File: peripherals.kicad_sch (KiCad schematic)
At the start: 27 parts, among them J7 Conn_01x04, J8 Conn_01x06, J9 Conn_01x06, U11 TB6612FNG, U2 LSM6DSV

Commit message: Use basic parts where possible
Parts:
- C2, C32, C36, C37, C38, C39: footprint Capacitor_SMD:C_0603_1608Metric_Pad1.08x0.95mm_HandSolder -> Capacitor_SMD:C_0603_1608Metric
- R19: footprint Resistor_SMD:R_0603_1608Metric_Pad0.98x0.95mm_HandSolder -> Resistor_SMD:R_0603_1608Metric; LCSC PN C98220 -> C25804
- R20, R22, R23, R26, R27: footprint Resistor_SMD:R_0603_1608Metric_Pad0.98x0.95mm_HandSolder -> Resistor_SMD:R_0603_1608Metric; LCSC PN C185354 -> C4177
- R21, R24, R25, R28, R29: footprint Resistor_SMD:R_0603_1608Metric_Pad0.98x0.95mm_HandSolder -> Resistor_SMD:R_0603_1608Metric; LCSC PN C108078 -> C22978
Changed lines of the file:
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@@
 			)
 		)
-		(property "Footprint" "Resistor_SMD:R_0603_1608Metric_Pad0.98x0.95mm_HandSolder"
+		(property "Footprint" "Resistor_SMD:R_0603_1608Metric"
 			(at 69.088 160.02 90)
 			(effects
@@
 			)
 		)
-		(property "LCSC PN" "C108078"
+		(property "LCSC PN" "C22978"
 			(at 67.31 160.02 0)
 			(effects
@@
 			)
 		)
-		(property "Footprint" "Capacitor_SMD:C_0603_1608Metric_Pad1.08x0.95mm_HandSolder"
+		(property "Footprint" "Capacitor_SMD:C_0603_1608Metric"
 			(at 70.1548 53.34 0)
 			(effects
@@
 			)
 		)
-		(property "Footprint" "Resistor_SMD:R_0603_1608Metric_Pad0.98x0.95mm_HandSolder"
+		(property "Footprint" "Resistor_SMD:R_0603_1608Metric"
 			(at 56.388 129.54 90)
 			(effects
@@
 			)
 		)
-		(property "LCSC PN" "C108078"
+		(property "LCSC PN" "C22978"
 			(at 54.61 129.54 0)
 			(effects
@@
 			)
 		)
-		(property "Footprint" "Capacitor_SMD:C_0603_1608Metric_Pad1.08x0.95mm_HandSolder"
+		(property "Footprint" "Capacitor_SMD:C_0603_1608Metric"
 			(at 133.6548 119.38 0)
 			(effects
@@
 			)
 		)
-		(property "Footprint" "Resistor_SMD:R_0603_1608Metric_Pad0.98x0.95mm_HandSolder"
+		(property "Footprint" "Resistor_SMD:R_0603_1608Metric"
 			(at 143.002 46.99 90)
 			(effects
@@
 			)
 		)
-		(property "LCSC PN" "C98220"
+		(property "LCSC PN" "C25804"
 			(at 144.78 46.99 0)
 			(effects
@@
 			)
 		)
-		(property "Footprint" "Resistor_SMD:R_0603_1608Metric_Pad0.98x0.95mm_HandSolder"
+		(property "Footprint" "Resistor_SMD:R_0603_1608Metric"
 			(at 60.96 120.142 90)
 			(effects
@@
 			)
 		)
-		(property "LCSC PN" "C185354"
+		(property "LCSC PN" "C4177"
 			(at 60.96 121.92 90)
 			(effects
@@
 			)
 		)
-		(property "Footprint" "Capacitor_SMD:C_0603_1608Metric_Pad1.08x0.95mm_HandSolder"
+		(property "Footprint" "Capacitor_SMD:C_0603_1608Metric"
 			(at 228.2952 119.38 0)
 			(effects
@@
 			)
 		)
-		(property "Footprint" "Resistor_SMD:R_0603_1608Metric_Pad0.98x0.95mm_HandSolder"
+		(property "Footprint" "Resistor_SMD:R_0603_1608Metric"
 			(at 210.82 50.292 90)
 			(effects
@@
 			)
 		)
-		(property "LCSC PN" "C185354"
+		(property "LCSC PN" "C4177"
 			(at 210.82 52.07 90)
 			(effects
@@
 			)
 		)
-		(property "Footprint" "Resistor_SMD:R_0603_1608Metric_Pad0.98x0.95mm_HandSolder"
+		(property "Footprint" "Resistor_SMD:R_0603_1608Metric"
 			(at 60.96 150.622 90)
 			(effects
@@
 			)
 		)
-		(property "LCSC PN" "C185354"
+		(property "LCSC PN" "C4177"
 			(at 60.96 152.4 90)
 			(effects
@@
 			)
 		)
-		(property "Footprint" "Resistor_SMD:R_0603_1608Metric_Pad0.98x0.95mm_HandSolder"
+		(property "Footprint" "Resistor_SMD:R_0603_1608Metric"
 			(at 56.388 160.02 90)
 			(effects
@@
 			)
 		)
-		(property "LCSC PN" "C108078"
+		(property "LCSC PN" "C22978"
 			(at 54.61 160.02 0)
 			(effects
@@
 			)
 		)
-		(property "Footprint" "Resistor_SMD:R_0603_1608Metric_Pad0.98x0.95mm_HandSolder"
+		(property "Footprint" "Resistor_SMD:R_0603_1608Metric"
 			(at 206.248 57.15 90)
 			(effects
@@
 			)
 		)
-		(property "LCSC PN" "C108078"
+		(property "LCSC PN" "C22978"
 			(at 204.47 57.15 0)
 			(effects
@@
 			)
 		)
-		(property "Footprint" "Resistor_SMD:R_0603_1608Metric_Pad0.98x0.95mm_HandSolder"
+		(property "Footprint" "Resistor_SMD:R_0603_1608Metric"
 			(at 73.66 122.682 90)
 			(effects
@@
 			)
 		)
-		(property "LCSC PN" "C185354"
+		(property "LCSC PN" "C4177"
 			(at 73.66 124.46 90)
 			(effects
@@
 			)
 		)
-		(property "Footprint" "Capacitor_SMD:C_0603_1608Metric_Pad1.08x0.95mm_HandSolder"
+		(property "Footprint" "Capacitor_SMD:C_0603_1608Metric"
 			(at 215.5952 119.38 0)
 			(effects
@@
 			)
 		)
-		(property "Footprint" "Capacitor_SMD:C_0603_1608Metric_Pad1.08x0.95mm_HandSolder"
+		(property "Footprint" "Capacitor_SMD:C_0603_1608Metric"
 			(at 84.1248 53.34 0)
 			(effects
@@
 			)
 		)
-		(property "Footprint" "Resistor_SMD:R_0603_1608Metric_Pad0.98x0.95mm_HandSolder"
+		(property "Footprint" "Resistor_SMD:R_0603_1608Metric"
 			(at 69.088 129.54 90)
 			(effects
@@
 			)
 		)
-		(property "LCSC PN" "C108078"
+		(property "LCSC PN" "C22978"
 			(at 67.31 129.54 0)
 			(effects
@@
 			)
 		)
-		(property "Footprint" "Resistor_SMD:R_0603_1608Metric_Pad0.98x0.95mm_HandSolder"
+		(property "Footprint" "Resistor_SMD:R_0603_1608Metric"
 			(at 73.66 153.162 90)
 			(effects
@@
 			)
 		)
-		(property "LCSC PN" "C185354"
+		(property "LCSC PN" "C4177"
 			(at 73.66 154.94 90)
 			(effects
@@
 			)
 		)
-		(property "Footprint" "Capacitor_SMD:C_0603_1608Metric_Pad1.08x0.95mm_HandSolder"
+		(property "Footprint" "Capacitor_SMD:C_0603_1608Metric"
 			(at 120.9548 119.38 0)
 			(effects

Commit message: Sketch out component placement
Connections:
- net INT renamed INT1
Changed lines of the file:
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@@
 		)
 	)
-	(hierarchical_label "INT"
+	(hierarchical_label "INT1"
 		(shape output)
 		(at 156.21 52.07 0)

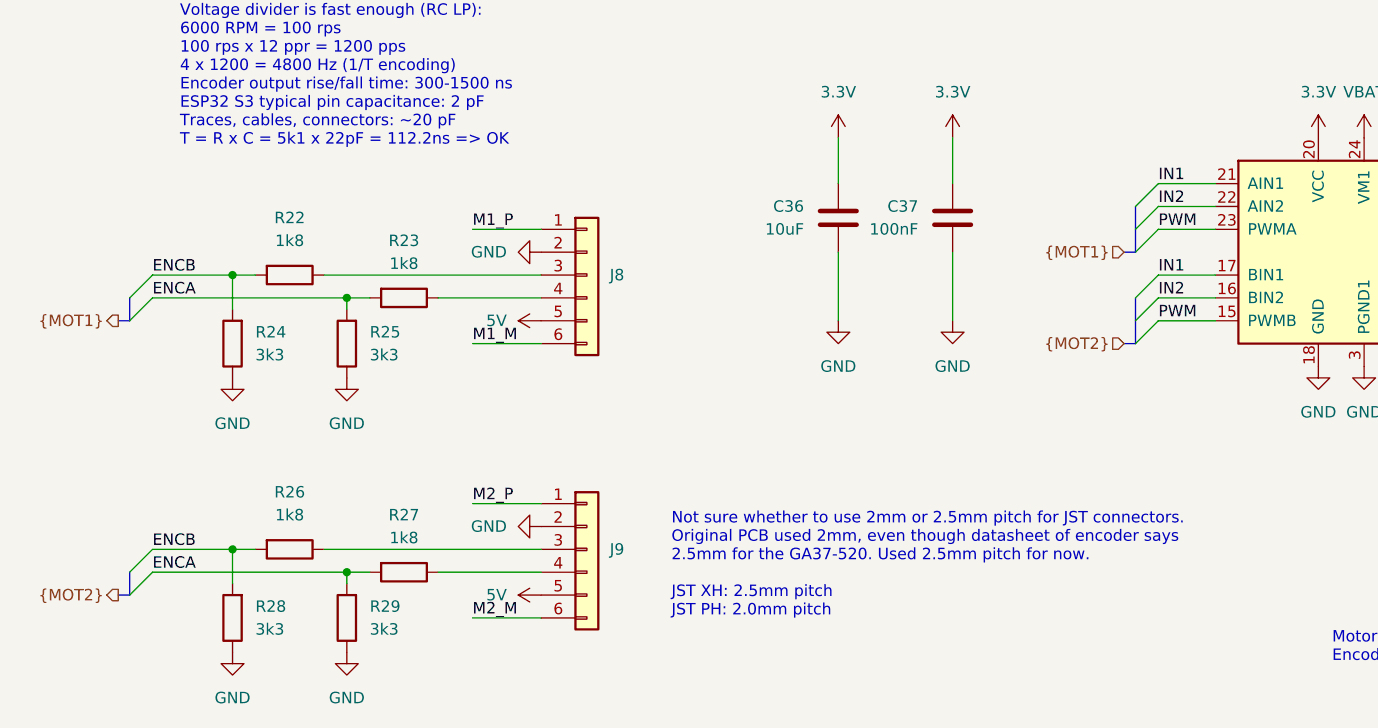
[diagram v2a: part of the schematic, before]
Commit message: Fix bus merging and add net classes
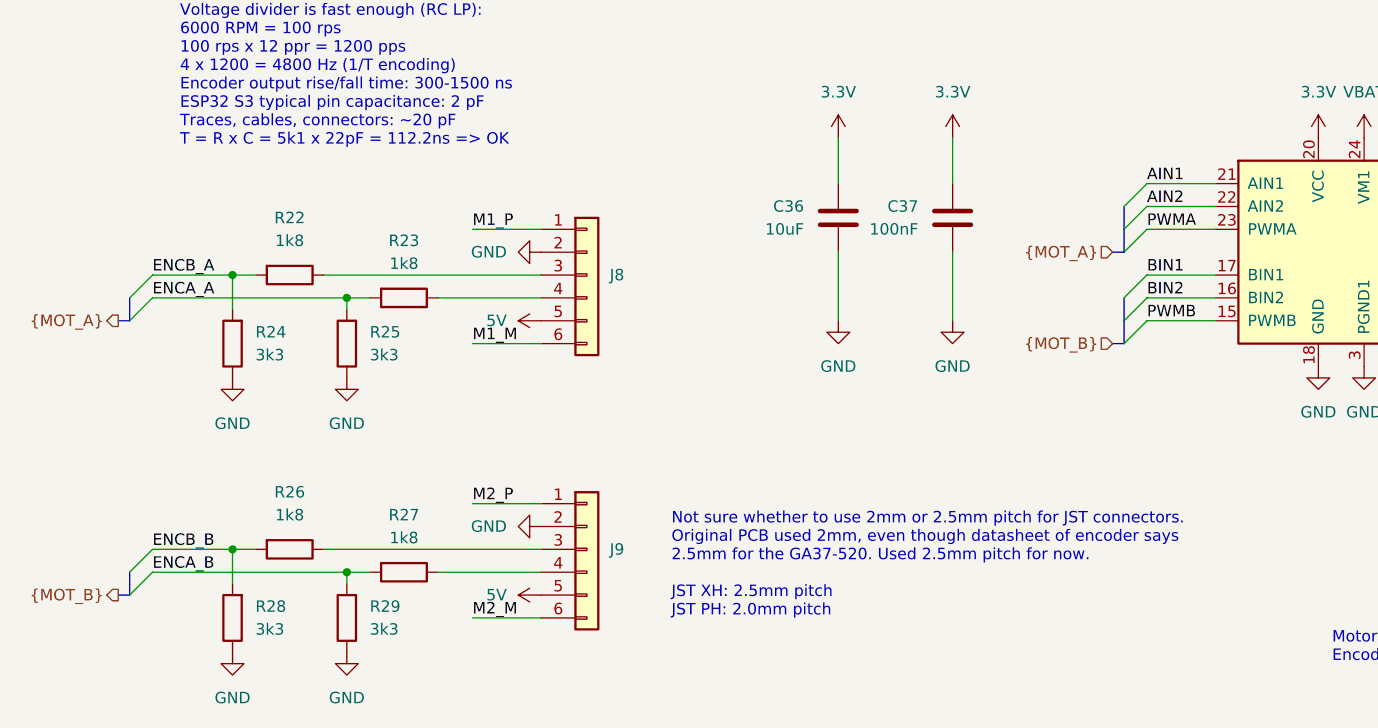
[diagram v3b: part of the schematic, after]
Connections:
- net ENCA renamed ENCA_A
- net ENCA_A: no longer R27.2, R29.2
- net ENCB renamed ENCB_A
- net ENCB_A: no longer R26.2, R28.2
- net IN1 renamed AIN1
- net AIN1: no longer U11.17 (BIN1)
- net IN2 renamed AIN2
- net AIN2: no longer U11.16 (BIN2)
- net PWM renamed PWMA
- net PWMA: no longer U11.15 (PWMB)
- new net BIN1: U11.17 (BIN1)
- new net BIN2: U11.16 (BIN2)
- new net ENCA_B: R27.2, R29.2
- new net ENCB_B: R26.2, R28.2
- new net PWMB: U11.15 (PWMB)

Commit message: Start conceptual layouting
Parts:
- TP10, TP11, TP12: footprint TestPoint:TestPoint_Pad_D1.5mm -> TestPoint:TestPoint_THTPad_D1.0mm_Drill0.5mm
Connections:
- net M1_M renamed M1_N
- net M2_M renamed M2_N
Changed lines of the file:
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@@
 		)
 	)
-	(label "M2_M"
+	(label "M2_N"
 		(at 200.66 121.92 180)
 		(effects
@@
 		)
 	)
-	(label "M2_M"
+	(label "M2_N"
 		(at 81.28 160.02 0)
 		(effects
@@
 		)
 	)
-	(label "M1_M"
+	(label "M1_N"
 		(at 81.28 129.54 0)
 		(effects
@@
 		)
 	)
-	(label "M1_M"
+	(label "M1_N"
 		(at 200.66 114.3 180)
 		(effects
@@
 			)
 		)
-		(property "Footprint" "TestPoint:TestPoint_Pad_D1.5mm"
+		(property "Footprint" "TestPoint:TestPoint_THTPad_D1.0mm_Drill0.5mm"
 			(at 219.71 48.26 0)
 			(effects
@@
 			)
 		)
-		(property "Footprint" "TestPoint:TestPoint_Pad_D1.5mm"
+		(property "Footprint" "TestPoint:TestPoint_THTPad_D1.0mm_Drill0.5mm"
 			(at 199.39 48.26 0)
 			(effects
@@
 			)
 		)
-		(property "Footprint" "TestPoint:TestPoint_Pad_D1.5mm"
+		(property "Footprint" "TestPoint:TestPoint_THTPad_D1.0mm_Drill0.5mm"
 			(at 158.75 49.53 0)
 			(effects

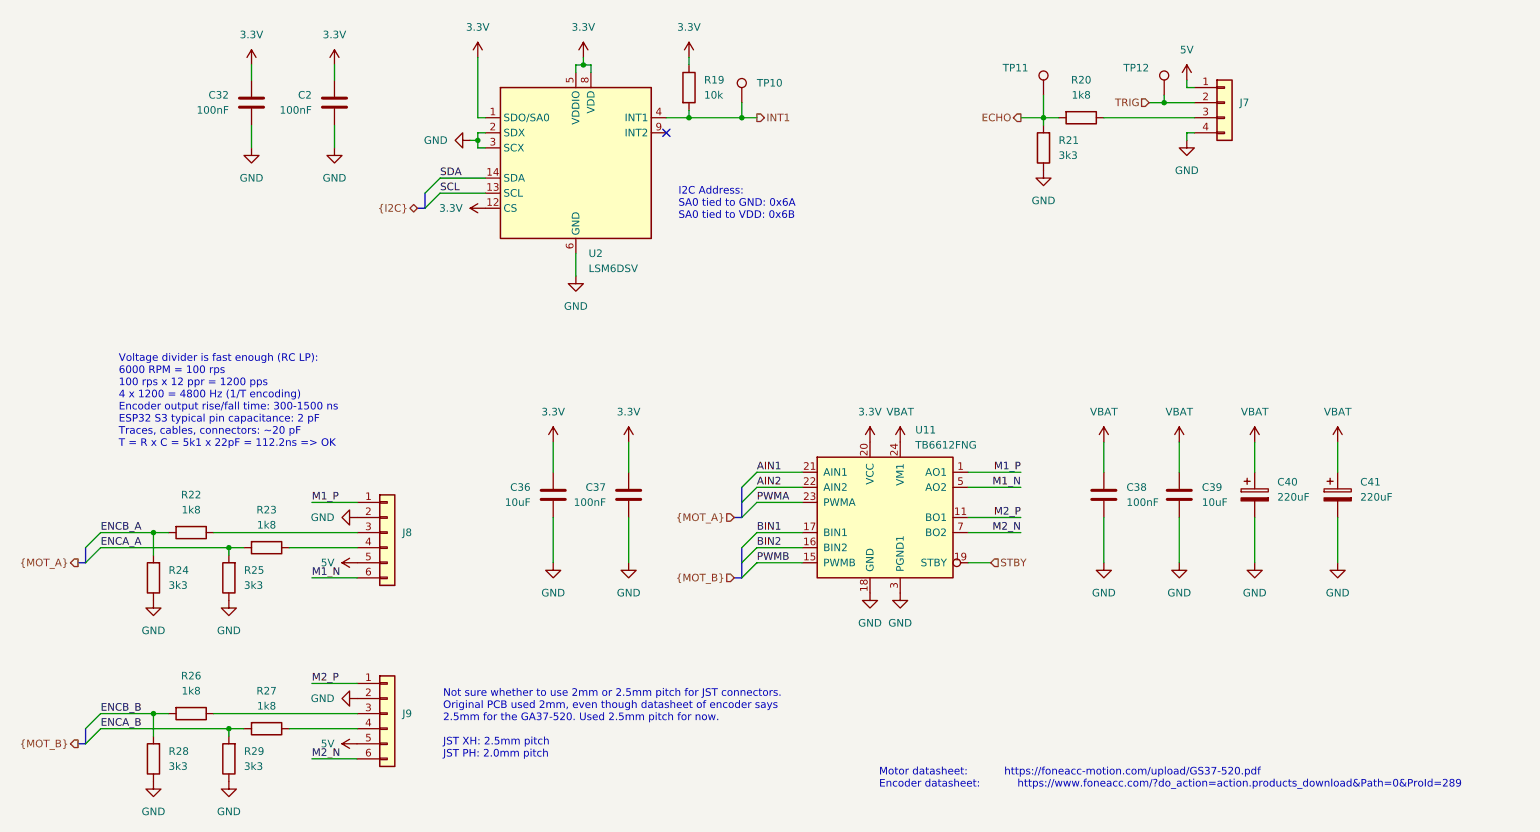
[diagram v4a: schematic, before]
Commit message: Continue layout and update schematic
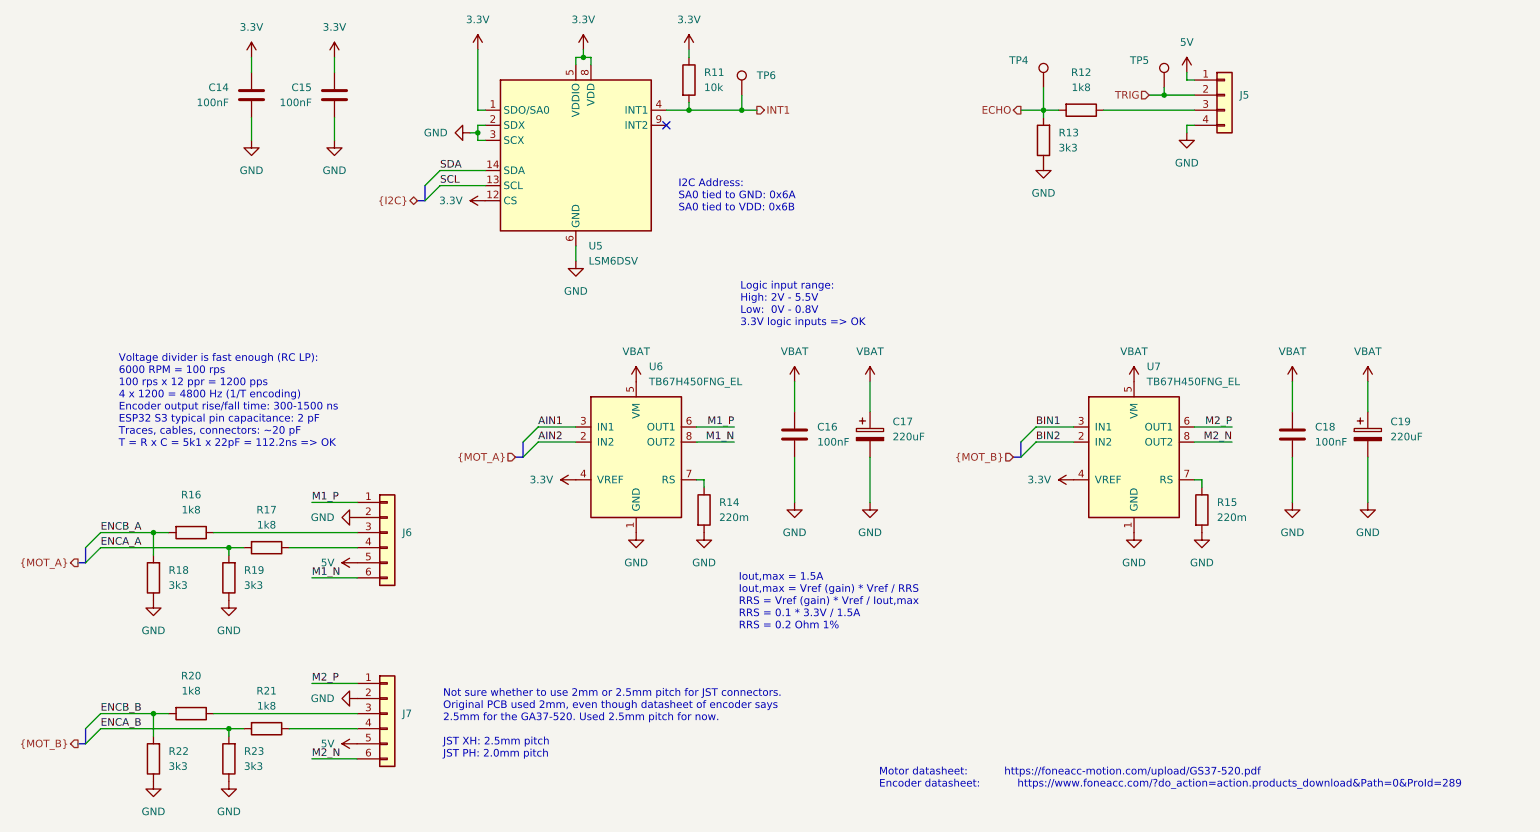
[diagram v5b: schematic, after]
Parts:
- removed C36, C39: 10uF, Capacitor_SMD:C_0603_1608Metric, symbol Device:C
- removed C37: 100nF, Capacitor_SMD:C_0603_1608Metric, symbol Device:C
- removed U11: TB6612FNG, Package_SO:SSOP-24_5.3x8.2mm_P0.65mm, symbol Driver_Motor:TB6612FNG
- added C16: 100nF, Capacitor_SMD:C_0603_1608Metric, symbol Device:C
- added R14, R15: 220m, Resistor_SMD:R_1210_3225Metric, symbol Device:R
- added U6, U7: TB67H450FNG_EL, Tumbler2:SOIC127P599X175-9N, symbol Tumbler2:TB67H450FNG_EL
- renumbered C32 to C14, C2 to C15, C41 to C17, C38 to C18, C40 to C19, J7 to J5, J8 to J6, J9 to J7, R19 to R11, R20 to R12, R21 to R13, R22 to R16, R23 to R17, R24 to R18, R25 to R19, R26 to R20, R27 to R21, R28 to R22, R29 to R23, TP11 to TP4, TP12 to TP5, TP10 to TP6, U2 to U5
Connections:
- net 3.3V: now also U6.4 (VREF), U7.4 (VREF)
- net AIN1: now also U6.3 (IN1)
- net AIN2: now also U6.2 (IN2)
- net BIN1: now also U7.3 (IN1)
- net BIN2: now also U7.2 (IN2)
- net GND: now also C16.2, R14.2, R15.2, U6.1 (GND), U6.9 (GND), U7.1 (GND), U7.9 (GND)
- net M1_N: now also U6.8 (OUT2)
- net M1_P: now also U6.6 (OUT1)
- net M2_N: now also U7.8 (OUT2)
- net M2_P: now also U7.6 (OUT1)
- net VBAT: now also C16.1, U6.5 (VM), U7.5 (VM)
- new net: R14.1, U6.7 (RS)
- new net: R15.1, U7.7 (RS)
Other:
- note added: "Iout,max = 1.5A Iout,max = Vref (gain) * Vref / RRS RRS = Vref (gain) * Vref / Iout,max RRS = 0.1 * 3.3V / 1.5A RRS = 0.2 Ohm 1%"
- note added: "Logic input range: High: 2V - 5.5V Low: 0V - 0.8V 3.3V logic inputs => OK"
- moved on the sheet: C14, C15, C17, C18, C19, J5, R11, R12, R13, TP4, TP5, TP6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

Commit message: Continue layout and add pin header protection
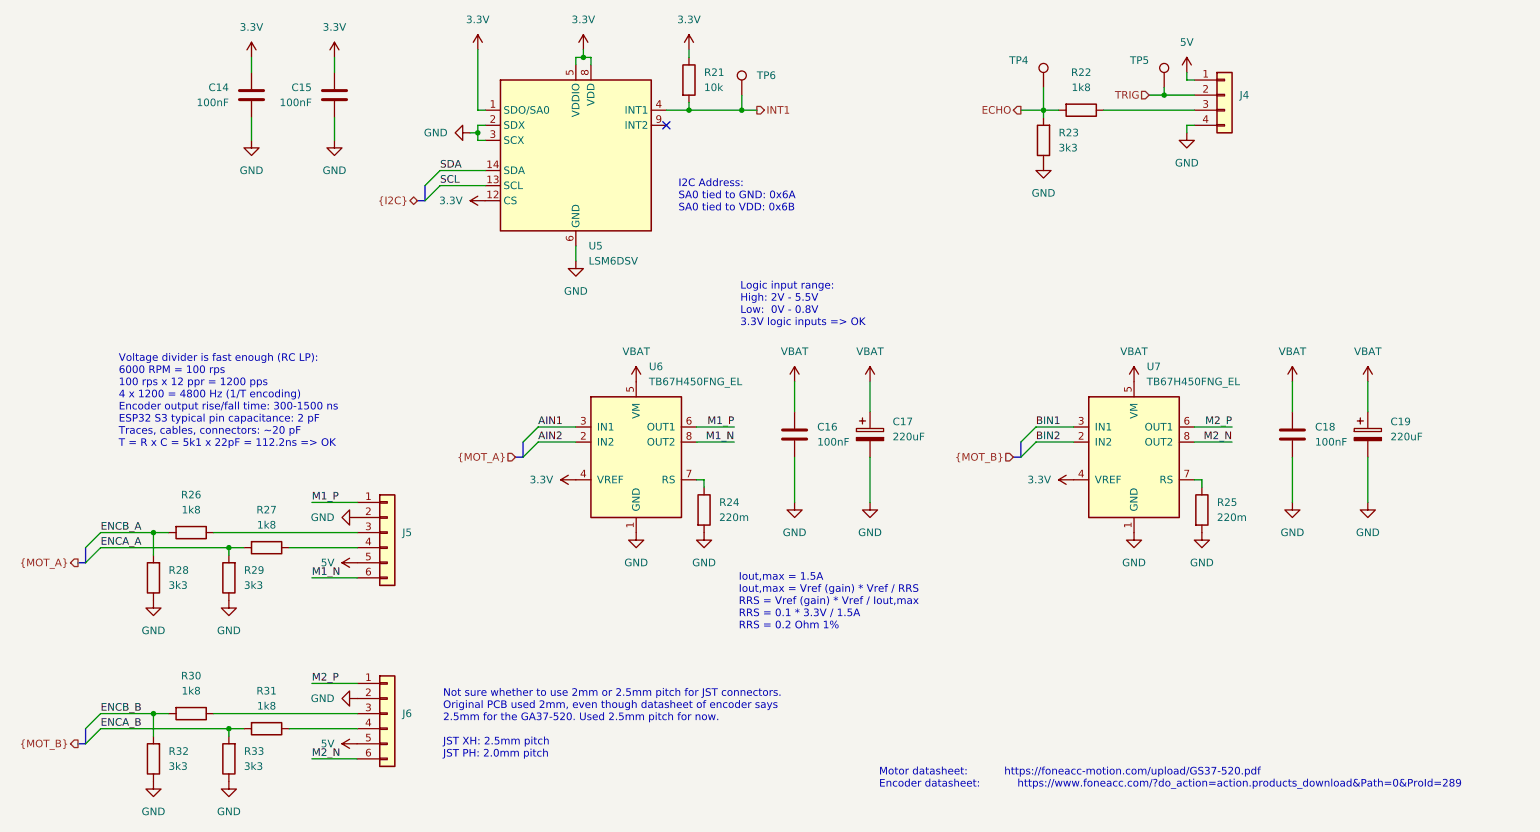
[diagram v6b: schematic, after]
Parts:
- renumbered J5 to J4, J6 to J5, J7 to J6, R11 to R21, R12 to R22, R13 to R23, R14 to R24, R15 to R25, R16 to R26, R17 to R27, R18 to R28, R19 to R29, R20 to R30, R21 to R31, R22 to R32, R23 to R33
